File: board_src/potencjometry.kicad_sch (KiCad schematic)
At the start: 8 parts, among them J13 Conn_01x03, Q1 NPN

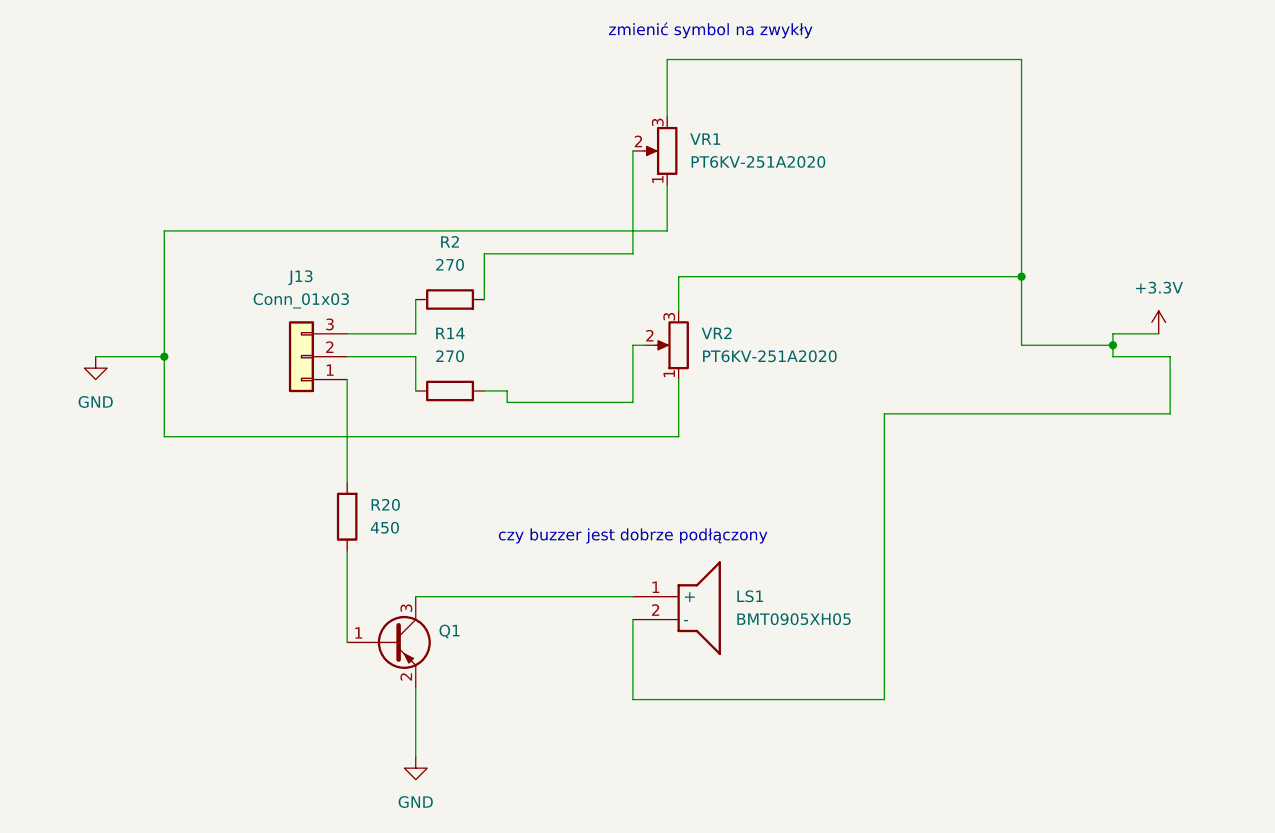
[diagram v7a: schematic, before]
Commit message: poprawione polaczenia diod i wartosci opornikow, aktualizacja niektorych elementow ze wzgledu na braki w magazynie
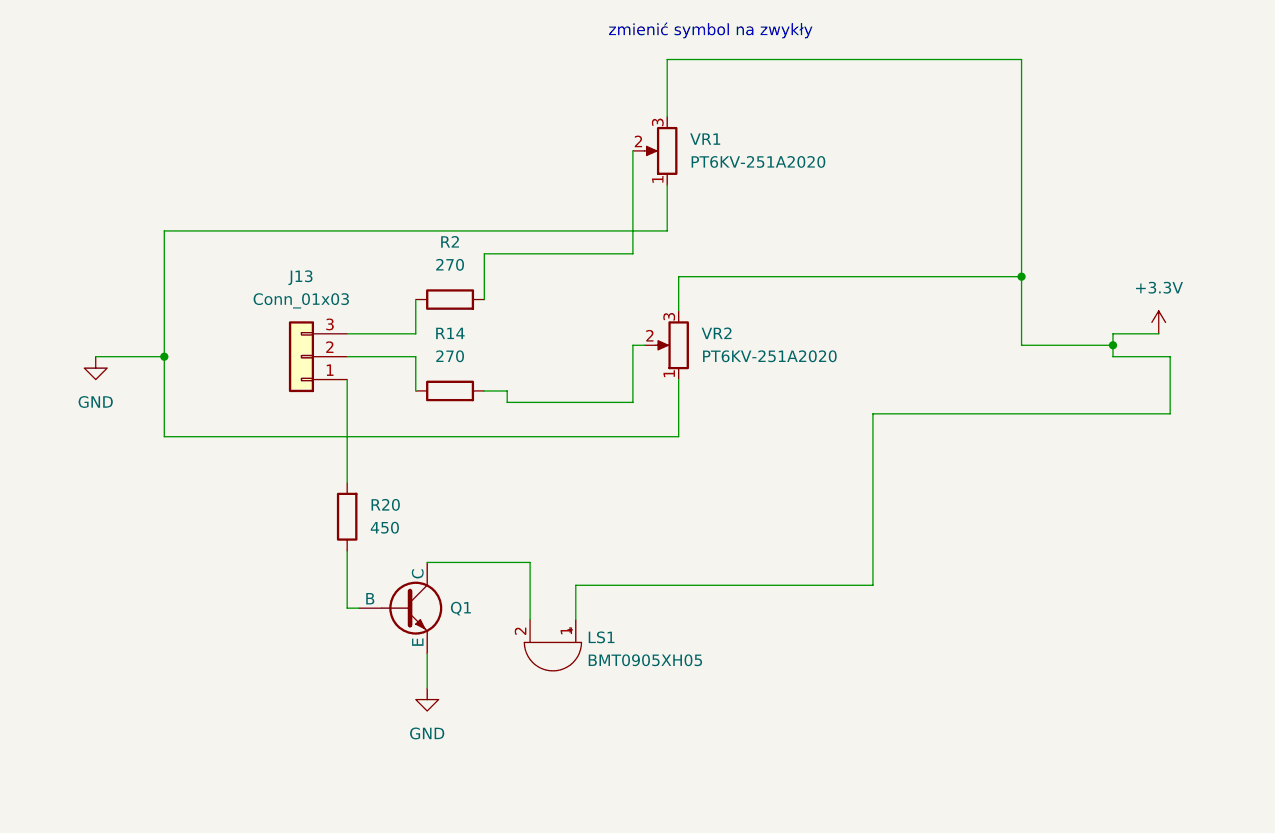
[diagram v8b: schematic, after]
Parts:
- LS1: symbol BMT0905XH05:BMT0905XH05 -> Device:Buzzer
- Q1: symbol Transistor_BJT:SS8550 -> Simulation_SPICE:NPN
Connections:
- net +3.3V: now also LS1.1 (+); no longer LS1.2 (-)
- net GND: now also Q1.3 (E); no longer Q1.2 (E)
- net at R20.1: now also Q1.2 (B); no longer Q1.1 (B)
- new net: LS1.2 (-), Q1.1 (C)
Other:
- note removed: "czy buzzer jest dobrze podłączony"
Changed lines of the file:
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@@
 	(generator_version "9.0")
 	(paper "A4")
-	(text "czy buzzer jest dobrze podłączony"
-		(exclude_from_sim no)
-		(at 113.03 108.966 0)
-		(effects
-			(font
-				(size 1.27 1.27)
-			)
-		)
-	)
 	(text "zmienić symbol na zwykły\n"
 		(exclude_from_sim no)
@@
 	(wire
 		(pts
-			(xy 113.03 127) (xy 140.97 127)
-		)
-		(stroke
-			(width 0)
-			(type default)
-		)
-	)
-	(wire
-		(pts
 			(xy 113.03 87.63) (xy 113.03 93.98)
 		)
@@
 	(wire
 		(pts
+			(xy 101.6 118.11) (xy 101.6 111.76)
+		)
+		(stroke
+			(width 0)
+			(type default)
+		)
+	)
+	(wire
+		(pts
 			(xy 166.37 86.36) (xy 171.45 86.36)
 		)
@@
 	(wire
 		(pts
+			(xy 81.28 116.84) (xy 82.55 116.84)
+		)
+		(stroke
+			(width 0)
+			(type default)
+		)
+	)
+	(wire
+		(pts
 			(xy 60.96 88.9) (xy 60.96 97.79)
 		)
@@
 	(wire
 		(pts
-			(xy 140.97 95.25) (xy 140.97 127)
+			(xy 139.7 95.25) (xy 139.7 114.3)
 		)
 		(stroke
@@
 	(wire
 		(pts
+			(xy 101.6 111.76) (xy 90.17 111.76)
+		)
+		(stroke
+			(width 0)
+			(type default)
+		)
+	)
+	(wire
+		(pts
 			(xy 172.72 88.9) (xy 166.37 88.9)
 		)
@@
 	(wire
 		(pts
-			(xy 88.9 115.57) (xy 113.03 115.57)
-		)
-		(stroke
-			(width 0)
-			(type default)
-		)
-	)
-	(wire
-		(pts
 			(xy 96.52 77.47) (xy 113.03 77.47)
 		)
@@
 	(wire
 		(pts
-			(xy 113.03 118.11) (xy 113.03 127)
+			(xy 90.17 121.92) (xy 90.17 125.73)
 		)
 		(stroke
@@
 	(wire
 		(pts
+			(xy 106.68 114.3) (xy 139.7 114.3)
+		)
+		(stroke
+			(width 0)
+			(type default)
+		)
+	)
+	(wire
+		(pts
 			(xy 166.37 88.9) (xy 166.37 87.63)
 		)
@@
 	(wire
 		(pts
-			(xy 172.72 95.25) (xy 140.97 95.25)
-		)
-		(stroke
-			(width 0)
-			(type default)
-		)
-	)
-	(wire
-		(pts
-			(xy 81.28 110.49) (xy 81.28 120.65)
+			(xy 172.72 95.25) (xy 139.7 95.25)
+		)
+		(stroke
+			(width 0)
+			(type default)
+		)
+	)
+	(wire
+		(pts
+			(xy 81.28 110.49) (xy 81.28 116.84)
 		)
 		(stroke
@@
 	(wire
 		(pts
-			(xy 88.9 125.73) (xy 88.9 133.35)
-		)
-		(stroke
-			(width 0)
-			(type default)
-		)
-	)
-	(wire
-		(pts
 			(xy 118.11 80.01) (xy 156.21 80.01)
 		)
@@
 		(pts
 			(xy 88.9 86.36) (xy 88.9 82.55)
+		)
+		(stroke
+			(width 0)
+			(type default)
+		)
+	)
+	(wire
+		(pts
+			(xy 106.68 114.3) (xy 106.68 118.11)
 		)
 		(stroke
@@
 	(symbol
 		(lib_id "power:GND")
-		(at 88.9 133.35 0)
+		(at 90.17 125.73 0)
 		(unit 1)
 		(exclude_from_sim no)
@@
 		(fields_autoplaced yes)
 		(property "Reference" "#PWR068"
-			(at 88.9 139.7 0)
+			(at 90.17 132.08 0)
 			(effects
 				(font
@@
 		)
 		(property "Value" "GND"
-			(at 88.9 138.43 0)
+			(at 90.17 130.81 0)
 			(effects
 				(font
@@
 		)
 		(property "Footprint" ""
-			(at 88.9 133.35 0)
+			(at 90.17 125.73 0)
 			(effects
 				(font
@@
 		)
 		(property "Datasheet" ""
-			(at 88.9 133.35 0)
+			(at 90.17 125.73 0)
 			(effects
 				(font
@@
 		)
 		(property "Description" "Power symbol creates a global label with name \"GND\" , ground"
-			(at 88.9 133.35 0)
+			(at 90.17 125.73 0)
 			(effects
 				(font
@@
 	)
 	(symbol
-		(lib_id "BMT0905XH05:BMT0905XH05")
-		(at 113.03 115.57 0)
+		(lib_id "Device:Buzzer")
+		(at 104.14 120.65 270)
 		(unit 1)
 		(exclude_from_sim no)
@@
 		(fields_autoplaced yes)
 		(property "Reference" "LS1"
-			(at 124.46 115.5699 0)
+			(at 107.95 120.135 90)
 			(effects
 				(font
@@
 		)
 		(property "Value" "BMT0905XH05"
-			(at 124.46 118.1099 0)
+			(at 107.95 122.675 90)
 			(effects
 				(font
@@
 		)
 		(property "Footprint" "footprints:BMT0905XH05"
-			(at 124.46 218.11 0)
+			(at 1.6 132.08 0)
 			(effects
 				(font
@@
 		)
 		(property "Datasheet" "https://www.tme.eu/Document/7f0b1b0d974635411dcfb4c191f1c3ad/BMT-0905XH05.pdf"
-			(at 124.46 318.11 0)
+			(at -98.4 132.08 0)
 			(effects
 				(font
@@
 		)
 		(property "Description" "Electro-magnetic Transducer"
-			(at 113.03 115.57 0)
+			(at 104.14 120.65 0)
 			(effects
 				(font
@@
 		)
 		(property "Height" "5"
-			(at 124.46 518.11 0)
+			(at -298.4 132.08 0)
 			(effects
 				(font
@@
 		)
 		(property "TME Electronic Components Part Number" ""
-			(at 124.46 618.11 0)
+			(at -398.4 132.08 0)
 			(effects
 				(font
@@
 		)
 		(property "TME Electronic Components Price/Stock" ""
-			(at 124.46 718.11 0)
+			(at -498.4 132.08 0)
 			(effects
 				(font
@@
 		)
 		(property "Manufacturer_Name" "BeStar Electronics"
-			(at 124.46 818.11 0)
+			(at -598.4 132.08 0)
 			(effects
 				(font
@@
 		)
 		(property "Manufacturer_Part_Number" "BMT0905XH05"
-			(at 124.46 918.11 0)
+			(at -698.4 132.08 0)
 			(effects
 				(font
@@
 	)
 	(symbol
-		(lib_id "Transistor_BJT:SS8550")
-		(at 86.36 120.65 0)
+		(lib_id "Simulation_SPICE:NPN")
+		(at 87.63 116.84 0)
 		(unit 1)
 		(exclude_from_sim no)
@@
 		(fields_autoplaced yes)
 		(property "Reference" "Q1"
-			(at 91.44 119.3799 0)
+			(at 92.71 116.8399 0)
 			(effects
 				(font
@@
 		)
 		(property "Value" "NPN"
-			(at 91.44 121.9199 0)
+			(at 92.71 118.1099 0)
 			(effects
 				(font
@@
 		)
 		(property "Footprint" "Package_TO_SOT_SMD:SOT-23"
-			(at 91.44 128.016 0)
-			(effects
-				(font
-					(size 1.27 1.27)
-					(italic yes)
-				)
-				(justify left)
-				(hide yes)
-			)
-		)
-		(property "Datasheet" "http://www.secosgmbh.com/datasheet/products/SSMPTransistor/SOT-23/SS8550.pdf"
-			(at 91.44 125.476 0)
-			(effects
-				(font
-					(size 1.27 1.27)
-				)
-				(justify left)
-				(hide yes)
-			)
-		)
-		(property "Description" "General Purpose PNP Transistor, 1.5A Ic, 25V Vce, SOT-23"
-			(at 120.396 122.936 0)
+			(at 151.13 116.84 0)
+			(effects
+				(font
+					(size 1.27 1.27)
+				)
+				(hide yes)
+			)
+		)
+		(property "Datasheet" "https://ngspice.sourceforge.io/docs/ngspice-html-manual/manual.xhtml#cha_BJTs"
+			(at 151.13 116.84 0)
+			(effects
+				(font
+					(size 1.27 1.27)
+				)
+				(hide yes)
+			)
+		)
+		(property "Description" "Bipolar transistor symbol for simulation only, substrate tied to the emitter"
+			(at 87.63 116.84 0)
 			(effects
 				(font
@@
 		)
 		(property "Sim.Device" "NPN"
-			(at 86.36 120.65 0)
+			(at 87.63 116.84 0)
 			(effects
 				(font
@@
 		)
 		(property "Sim.Type" "GUMMELPOON"
-			(at 86.36 120.65 0)
+			(at 87.63 116.84 0)
 			(effects
 				(font
@@
 		)
 		(property "Sim.Pins" "1=C 2=B 3=E"
-			(at 86.36 120.65 0)
-			(effects
-				(font
+			(at 87.63 116.84 0)
+			(effects
+				(font
